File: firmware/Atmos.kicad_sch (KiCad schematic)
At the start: 73 parts, among them J1 AS3935 breakout, J2 BME280 breakout, J3 USB_C_Receptacle_USB2.0_16P, J4 Micro_SD_Card, J5 Solar power input, J6 Amphenol 132134, Q1 PMOS_Substrate, Q2 PMOS_Substrate, Q3 PMOS_Substrate, SW2 SW_Push, U1 ESP32-S3-WROOM-1, U10 TPS22918DBVR, U11 MAX17048G_T10, U12 CN3791, U13 SGP40-D-R4, U2 AP2112K-3.3, U3 DS3231M, U4 PMS5003, U5 LTC4412xS6, U7 RFM95W-915S2, U8 USBLC6-2SC6, U9 TPS61023DRLR

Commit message: Cap fixes: C12 VG 1uF, +5V 2nd 22uF (C22), +5V_PMS bulk (C23), VBUS/VBAT/VSOL bulk
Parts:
- added C22, C23: 22uF, Capacitor_SMD:C_0805_2012Metric, symbol Device:C_US
- added C24: 4.7uF, Capacitor_SMD:C_0603_1608Metric, symbol Device:C_US
- added C25: 0.1uF, Capacitor_SMD:C_0603_1608Metric, symbol Device:C_US
- added C26: 10uF, Capacitor_SMD:C_0805_2012Metric, symbol Device:C_US
- C12: value 100nF -> 1uF
- L2: footprint Inductor_SMD:L_Coilcraft_1008HQ_2520Metric -> Inductor_SMD:L_Bourns-SRN4018
- R12: value 10k -> 12k
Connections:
- net +3V3: no longer R8.1
- net +5V: now also C22.2
- net +5V_PMS: now also C23.2
- net GND: now also D1.1 (K), C22.1, C23.1, C24.1, C25.1, C26.1; no longer D1.2 (A)
- net IO14: now also U1.22 (IO14)
- net IO15: now also U1.8 (IO15)
- net IO16: now also U1.9 (IO16)
- net VBUS: now also C24.2
- net VSOL: now also C26.2
- net at BT1.1 (+), U3.14 (VBAT): now also C25.2
- net at R8.2: now also D1.2 (A); no longer D1.1 (K)
- net STATUS_LED: now reaches U1.23 (IO21)
- net STATUS_LED: now also R8.1
- no-connect marks 45 -> 41
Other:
- moved on the sheet: D1

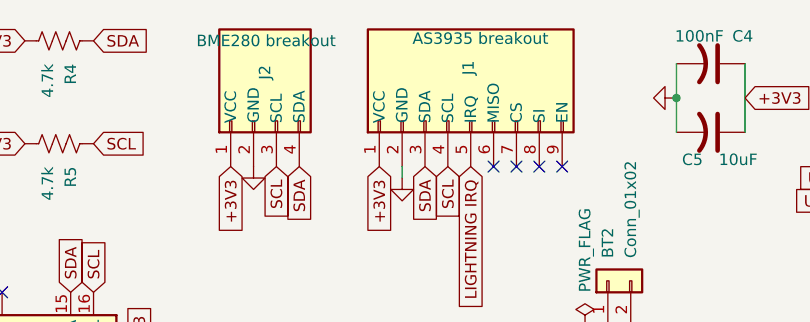
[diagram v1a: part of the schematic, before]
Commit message: BOM: specify Playing With Fusion SEN-39003 for AS3935 (J1); avoid Amazon clones
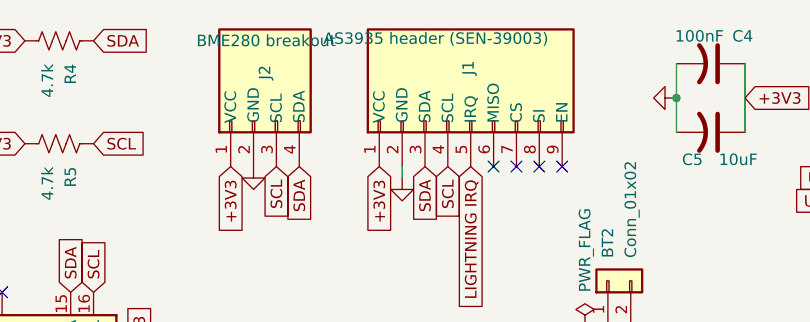
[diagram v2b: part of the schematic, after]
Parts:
- J1: value AS3935 breakout -> AS3935 header (SEN-39003)
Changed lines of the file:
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@@
 			)
 		)
-		(property "Value" "AS3935 breakout"
+		(property "Value" "AS3935 header (SEN-39003)"
 			(at 115.316 14.986 90)
 			(effects
